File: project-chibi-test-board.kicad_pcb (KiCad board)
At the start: 4 copper layers, 104.1 x 134.6 mm, 226 parts, among them J1 Conn_01x04, J10 Conn_01x02, J11 Conn_01x02, J12 Conn_02x06_Top_Bottom, J13 Conn_02x06_Top_Bottom, J14 Conn_02x06_Top_Bottom, J15 Conn_02x06_Top_Bottom, J16 Conn_01x02, J17 Conn_01x02, J18 Conn_Coaxial, J19 Conn_Coaxial, J2 Conn_Coaxial, J20 Conn_01x03, J21 Conn_01x03, J22 Conn_01x04, J23 USB_B_Micro, J24 Conn_01x06, J25 Conn_01x04, J26 Conn_Coaxial, J27 Conn_Coaxial, J28 Conn_01x03, J29 Conn_01x03, J3 Conn_Coaxial, J30 Conn_01x02, J31 Conn_01x02, J32 Conn_02x06_Top_Bottom, J33 Conn_02x06_Top_Bottom, J34 Conn_02x06_Top_Bottom, J35 Conn_02x06_Top_Bottom, J36 Conn_02x06_Top_Bottom, J37 Conn_02x06_Top_Bottom, J38 Conn_02x06_Top_Bottom, J39 Conn_02x06_Top_Bottom, J4 Conn_01x03, J40 Conn_01x02, J41 Conn_01x02, J42 Conn_Coaxial, J43 Conn_Coaxial, J44 Conn_01x04, J45 Conn_01x03, J46 Conn_01x03, J47 Conn_01x06, J48 Conn_01x02, J49 Conn_01x02, J5 Conn_01x03, J50 Conn_01x02, J51 Conn_01x02, J52 Conn_01x02, J6 Conn_02x06_Top_Bottom, J7 Conn_02x06_Top_Bottom, J8 Conn_02x06_Top_Bottom, J9 Conn_01x06, SW1 SW_DIP_x08, SW2 SW_DIP_x08, U1 40 MHz, U10 5M240ZT144C5N, U11 5M1270ZF256C5N, U2 2.048 MHz, U3 5M40ZE64C5N, U4 5M2210ZF256C5N, U5 93LC56BT-OT, U6 5M240ZT144C5N, U7 LM1117-3.3, U8 LM1117-1.8, U9 FT232H, Y1 12 MHz

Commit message: rough draft routing
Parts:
- C1, C2: moved to B.Cu
- moved R2 3.77 mm to (80.3, 141.4), turned to 0 degrees
- moved C1 3.72 mm to (81.9, 137.8)
- moved R1 3.59 mm to (84.7, 141.4), turned to 0 degrees
- moved C2 1.18 mm to (86.4, 137.8)
- moved U2 1.17 mm to (81.9, 139.1)
- moved U1 1.07 mm to (86.4, 139.1)
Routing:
- net /CLK_40MHZ: track 1.98 -> 369.0 mm, vias 1 -> 6
- net /CLK_2.048MHZ: track 1.93 -> 362.1 mm, vias 1 -> 8
- net Net-(D11-Pad2): track 0.00 -> 193.4 mm, vias 0 -> 7
- net Net-(R18-Pad1): track 0.00 -> 105.3 mm, vias 0 -> 4
- net Net-(D10-Pad1): track 0.00 -> 92.2 mm, vias 0 -> 2
- net /jtag-iface/MUX_TCK: track 0.00 -> 20.4 mm, vias 0 -> 1
- net /jtag-iface/MUX_TDI: track 0.00 -> 20.3 mm, vias 0 -> 1
- net /jtag-iface/MUX_TDO: track 0.00 -> 20.1 mm, vias 0 -> 1
- net /jtag-iface/MUX_TMS: track 0.00 -> 13.1 mm, vias 0 -> 1
- net GND: track 266.7 -> 276.3 mm, vias 107 -> 110
- net +3V3: track 135.9 -> 143.7 mm, vias 61 -> 63
- net Net-(D12-Pad1): track 0.00 -> 1.85 mm
- net /tgt-13x20/CLK1: track 41.0 -> 39.4 mm
- net Net-(D11-Pad1): track 0.00 -> 1.52 mm
- net Net-(R1-Pad2): track 0.00 -> 1.50 mm
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
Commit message: tweaks
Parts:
- moved C9 2.00 mm to (72.8, 69.8)
- moved C97 1.75 mm to (78.2, 77.8)
- moved C11 1.52 mm to (71.8, 77.8), turned to 90 degrees
- moved C10 1.50 mm to (76.0, 74.0)
- moved C12 1.50 mm to (71.8, 69.8)
- moved C8 1.50 mm to (70.8, 77.8)
- moved U3 1.50 mm to (72.0, 73.5)
- moved C7 1.27 mm to (68.2, 73.8)
- moved J2 1.27 mm to (72.4, 88.9)
- moved J3 1.27 mm to (81.3, 88.9)
- moved J4 1.27 mm to (69.8, 82.5)
- moved J5 1.27 mm to (78.7, 82.5)
- moved C98 1.06 mm to (66.5, 77.8)
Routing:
- net /CLK_40MHZ: track 369.0 -> 337.5 mm
- net /CLK_2.048MHZ: track 362.1 -> 343.3 mm, vias 8 -> 6
- net /tgt-4x6/ADBUS4: track 41.6 -> 33.9 mm, vias 2 -> 0
- net /tgt-4x6/ADBUS5: track 40.6 -> 33.2 mm, vias 2 -> 0
- net /tgt-4x6/ADBUS6: track 39.5 -> 32.6 mm, vias 2 -> 0
- net /tgt-4x6/ADBUS7: track 38.7 -> 32.0 mm, vias 2 -> 0
- net /tgt-4x6/JTAG_TDO: track 37.6 -> 31.4 mm, vias 2 -> 0
- net /tgt-4x6/ACBUS3: track 47.9 -> 41.9 mm
- net /tgt-4x6/ACBUS2: track 43.9 -> 38.2 mm, vias 2 -> 0
- net Net-(J1-Pad3): track 24.4 -> 18.7 mm
- net Net-(J1-Pad2): track 22.4 -> 16.7 mm
- net /tgt-4x6/ACBUS1: track 44.4 -> 38.8 mm, vias 2 -> 0
- net /tgt-4x6/ACBUS6: track 49.0 -> 43.5 mm
- net /tgt-4x6/ACBUS4: track 46.5 -> 41.1 mm, vias 2 -> 0
- net /tgt-4x6/ACBUS0: track 45.8 -> 40.5 mm, vias 2 -> 0
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
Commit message: more tweaks
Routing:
- net /CLK_40MHZ: track 337.5 -> 331.1 mm
- net /tgt-13x20/CLK1: track 39.4 -> 45.2 mm
- net /CLK_2.048MHZ: track 343.3 -> 339.3 mm
- net Net-(D11-Pad2): track 193.3 -> 195.4 mm
- net /tgt-7x12/JTAG_TDO: track 61.4 -> 59.9 mm
- net /tgt-13x20/ADBUS4: track 25.1 -> 23.7 mm
- net /tgt-13x20/ADBUS5: track 24.3 -> 23.0 mm
- net /tgt-7x12/JTAG_TCK: track 61.6 -> 60.5 mm
- net /tgt-7x12/ACBUS5: track 37.5 -> 36.5 mm
- net Net-(D10-Pad1): track 92.2 -> 93.3 mm
- net /tgt-7x12/ACBUS6: track 39.2 -> 38.4 mm
- net /tgt-13x20/EXPAND3_4: track 25.1 -> 24.4 mm
- net /tgt-7x12/JTAG_TDI: track 61.8 -> 61.1 mm
- net /tgt-7x12/JTAG_TMS: track 61.9 -> 61.2 mm
- net /tgt-13x20/ADBUS2: track 23.8 -> 23.2 mm
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
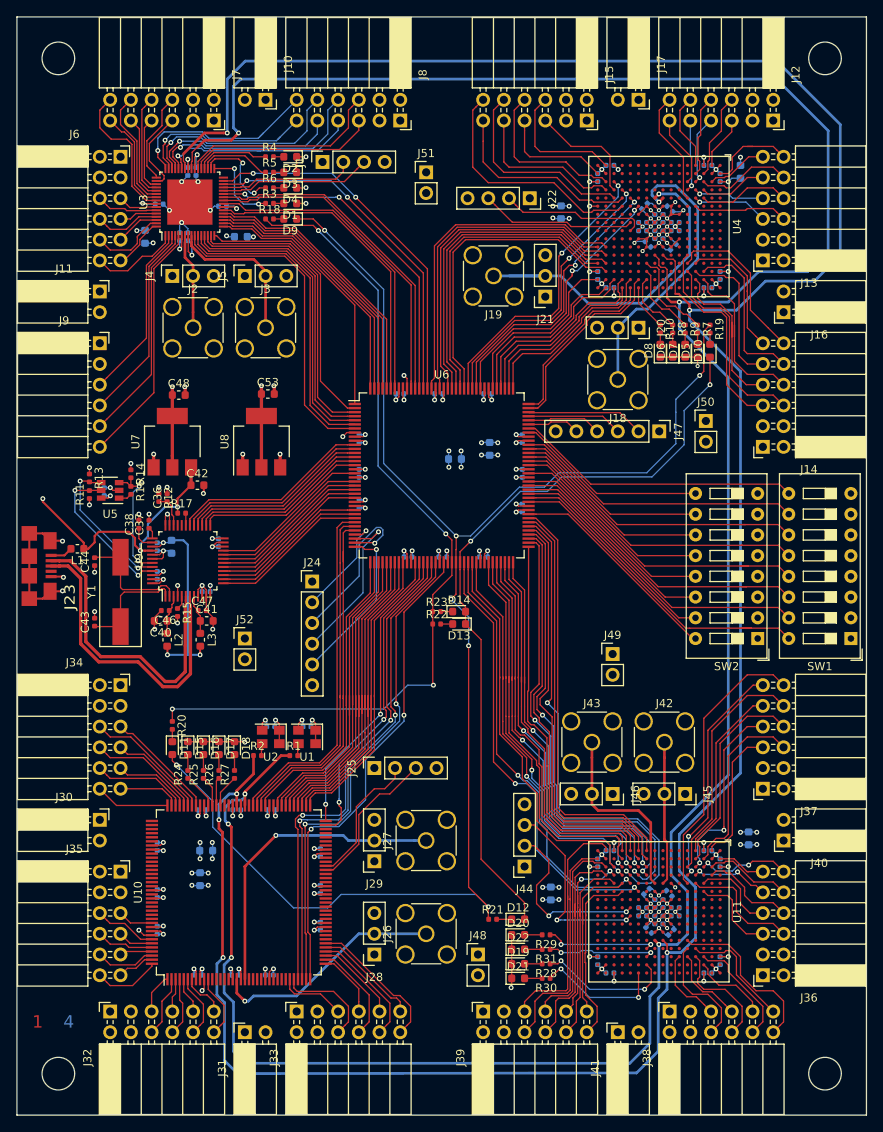
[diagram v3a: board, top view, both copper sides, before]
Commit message: front silk cleanup
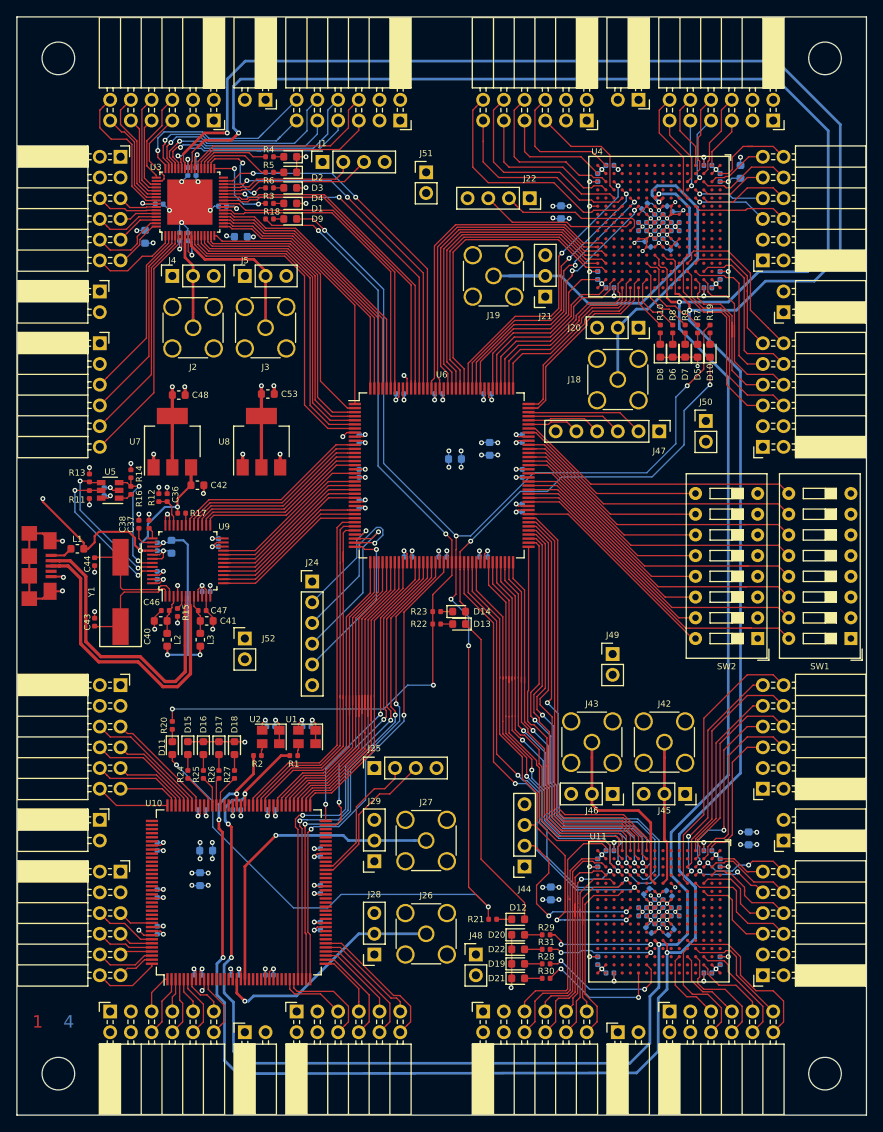
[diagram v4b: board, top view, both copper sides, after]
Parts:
- moved J48 0.25 mm to (107.1, 165.7)
